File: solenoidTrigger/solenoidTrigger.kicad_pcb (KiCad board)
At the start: 2 copper layers, 88.9 x 88.9 mm, 45 parts, among them J8 CONN_02X03, P1 OSTTC03, P2 OSTTC02, P3 OSTTC08, P4 OSTTC03, P5 OSTTC03, Q1 NMOS_CDS16, Q2 NMOS_CDS16, Q3 NMOS_CDS16, Q4 NMOS_CDS16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

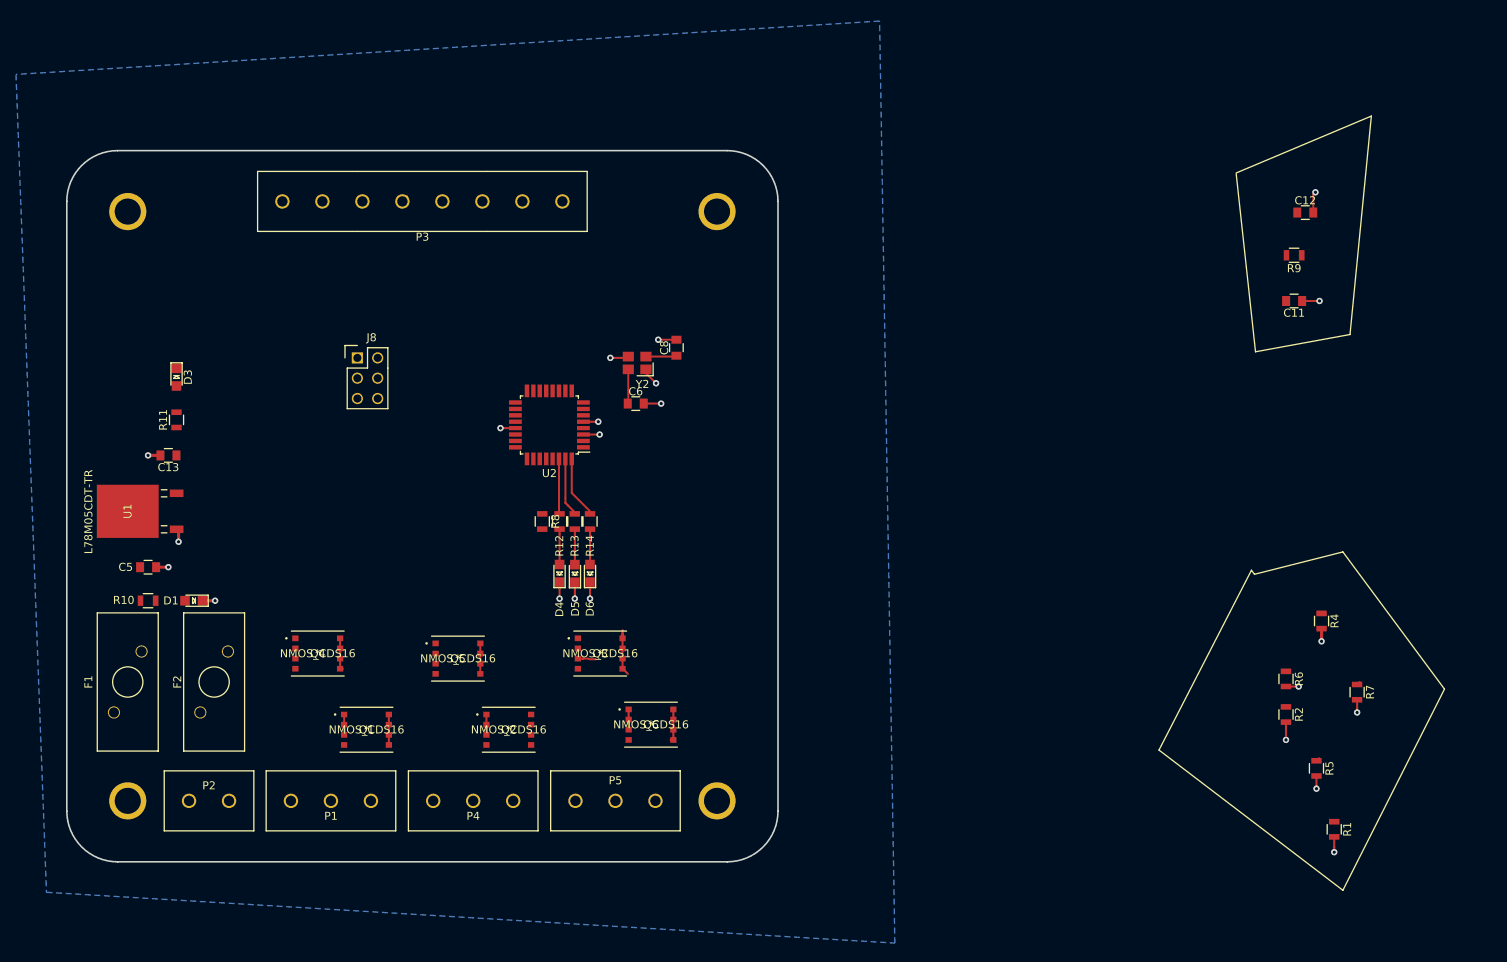
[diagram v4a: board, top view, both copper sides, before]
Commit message: continued moving around components
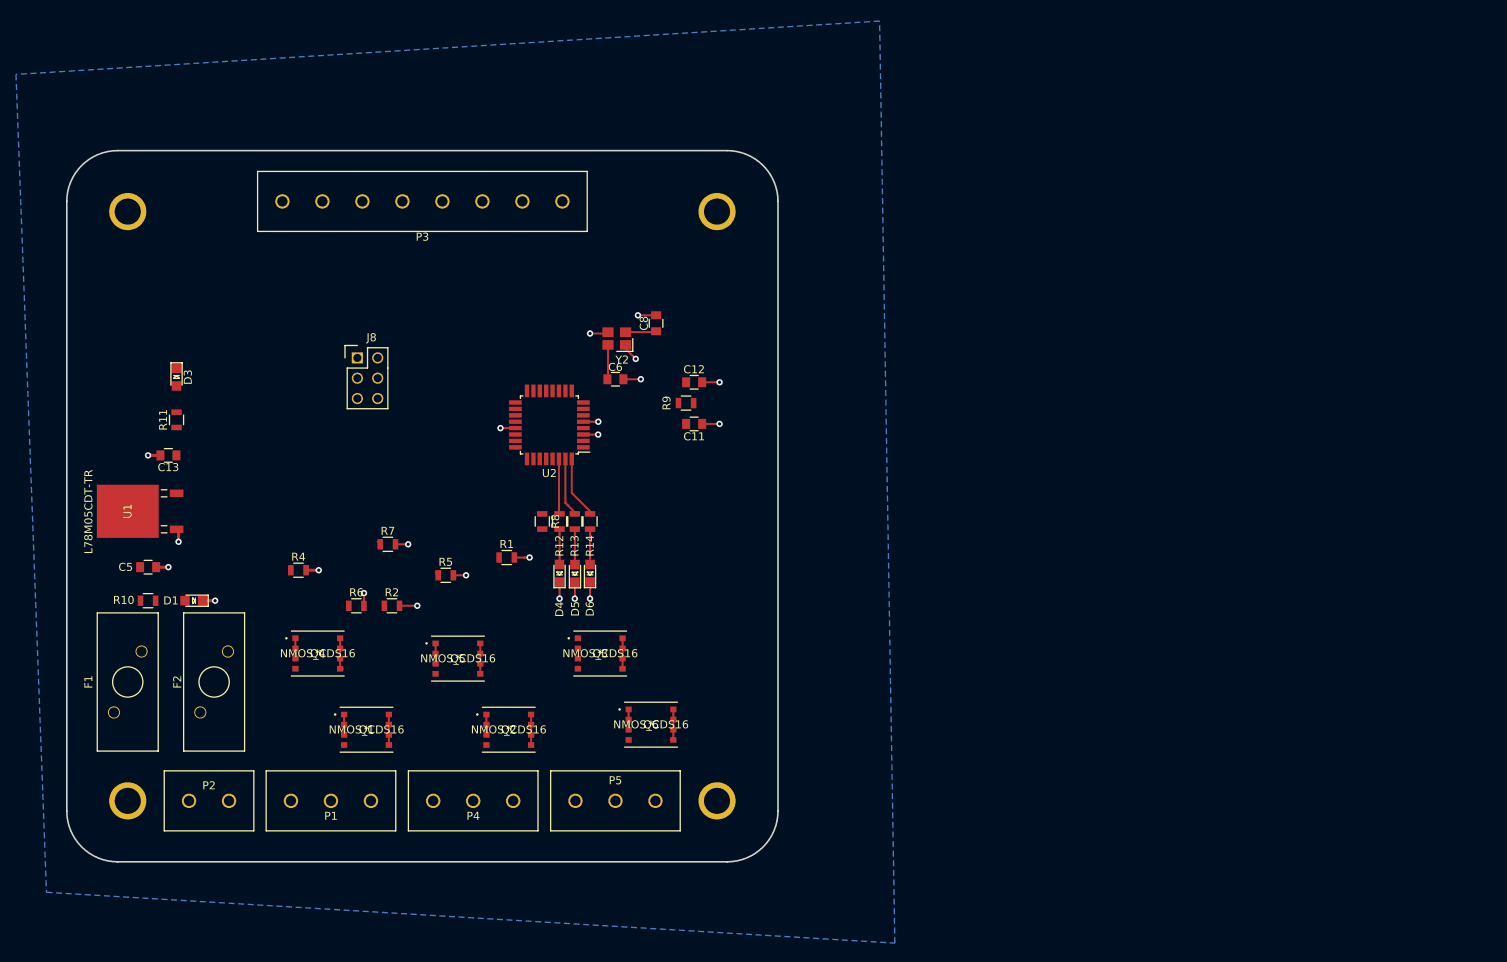
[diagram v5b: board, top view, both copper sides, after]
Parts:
- moved R4 128.0 mm to (131.8, 102.0), turned to 0 degrees
- moved R7 122.6 mm to (143.0, 98.7), turned to 0 degrees
- moved R6 116.6 mm to (139.1, 106.4), turned to 0 degrees
- moved R2 112.6 mm to (143.5, 106.4), turned to 0 degrees
- moved R5 111.5 mm to (150.2, 102.6), turned to 0 degrees
- moved R1 108.9 mm to (157.9, 100.4), turned to 0 degrees
- moved C12 79.3 mm to (181.3, 78.5)
- moved R9 78.2 mm to (180.3, 81.1)
- moved C11 76.6 mm to (181.3, 83.7)
- moved C6 3.97 mm to (171.4, 78.1)
- moved C8 3.97 mm to (176.5, 71.1)
- moved Y2 3.97 mm to (171.6, 73.0)
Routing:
- net /12V_Solenoid2: track 2.54 -> 5.08 mm
- net /12V_Solenoid1: track 2.54 -> 5.08 mm
- net /12V_Solenoid3: track 4.64 -> 2.54 mm
- net /12V_Switch: track 22.4 -> 23.7 mm
- net GND: track 42.8 -> 42.2 mm

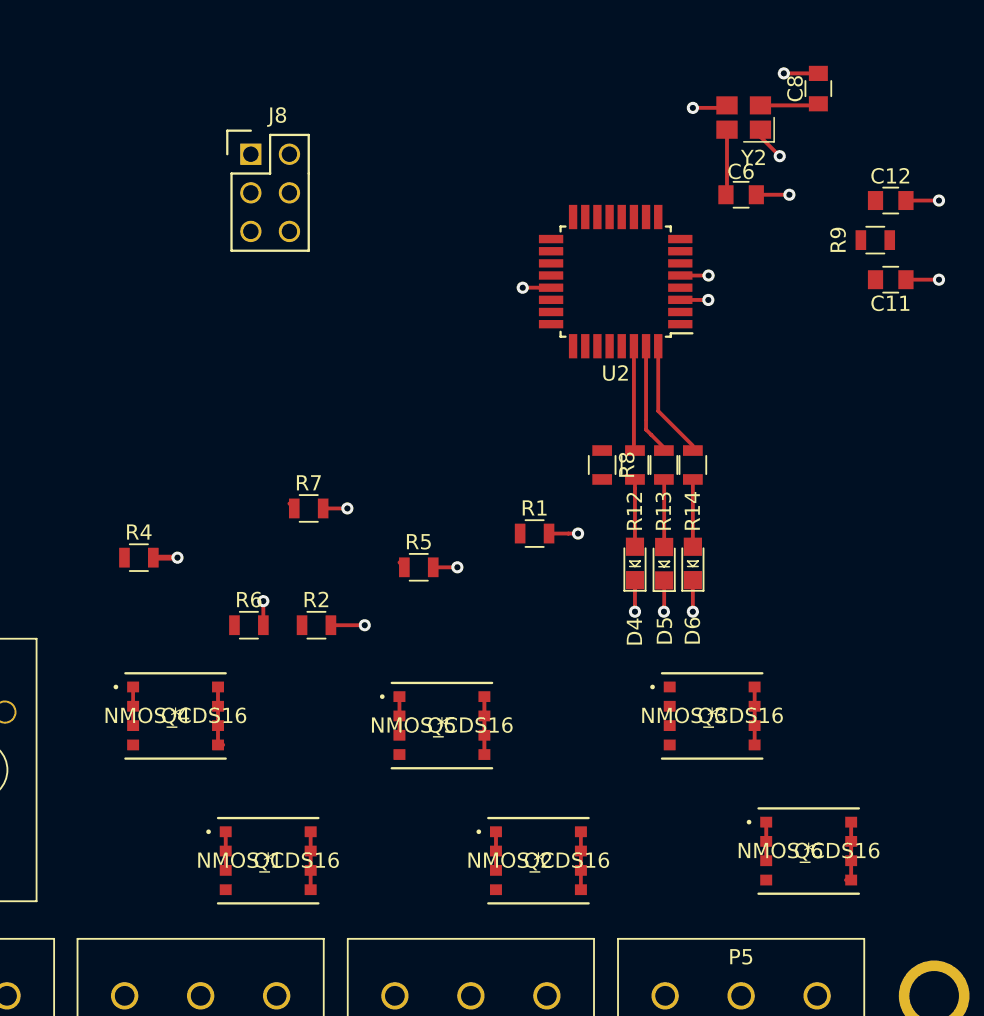
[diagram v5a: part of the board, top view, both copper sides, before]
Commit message: moved all components into what seems to be resonable positions, waiting for confirmation from Will before adding traces/vias
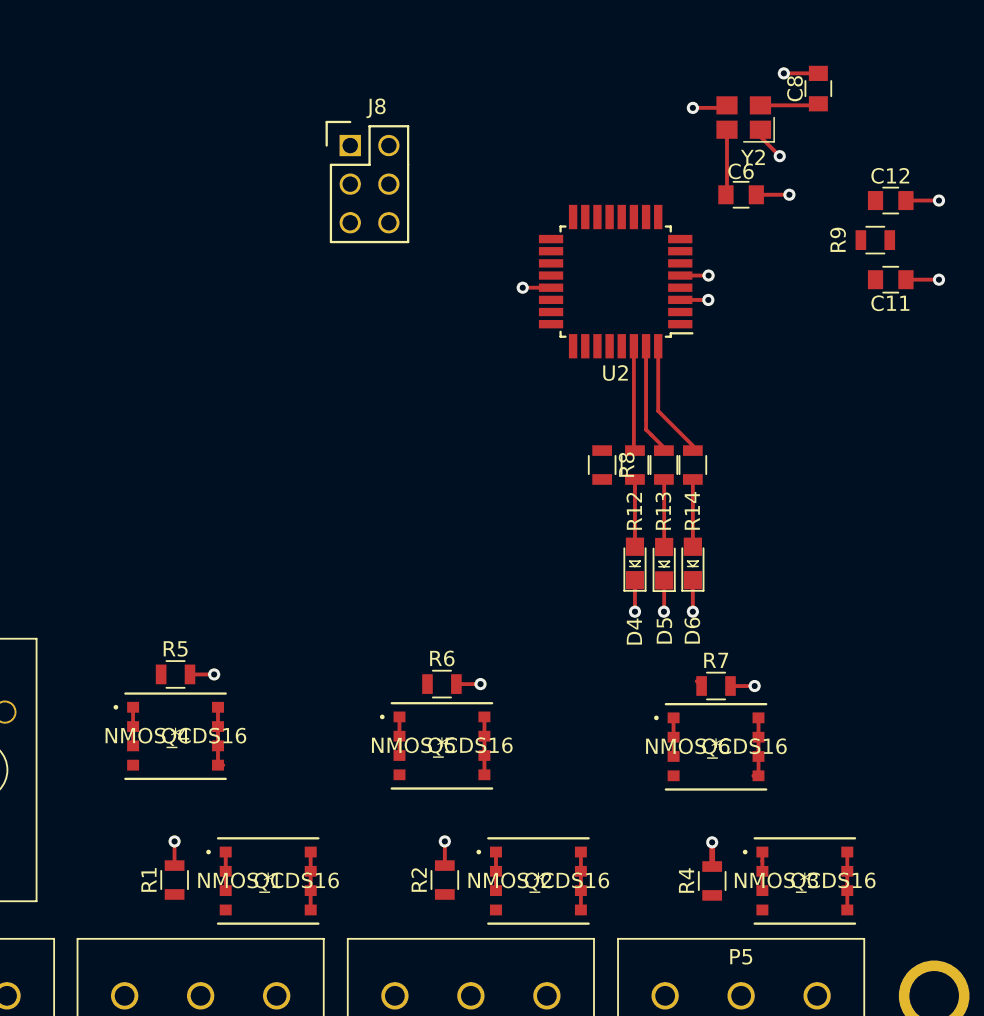
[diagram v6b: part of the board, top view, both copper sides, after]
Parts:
- moved R4 43.3 mm to (169.5, 123.3), turned to 90 degrees
- moved R1 32.9 mm to (134.2, 123.2), turned to 90 degrees
- moved R7 29.2 mm to (169.8, 110.4)
- moved R2 18.8 mm to (152.0, 123.2), turned to 90 degrees
- moved R5 17.5 mm to (134.2, 109.7)
- moved R6 13.3 mm to (151.8, 110.3)
- moved Q3 12.5 mm to (175.6, 123.3)
- moved Q6 9.18 mm to (169.8, 114.4)
- moved J8 6.57 mm to (145.7, 74.9)
- moved Q1 1.33 mm to (140.3, 123.3)
- moved Q2 1.33 mm to (158.1, 123.3)
- moved Q4 1.33 mm to (134.2, 113.7)
- moved Q5 1.33 mm to (151.8, 114.4)
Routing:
- net /12V_Solenoid3: track 2.54 -> 5.08 mm
- net GND: track 42.2 -> 41.2 mm

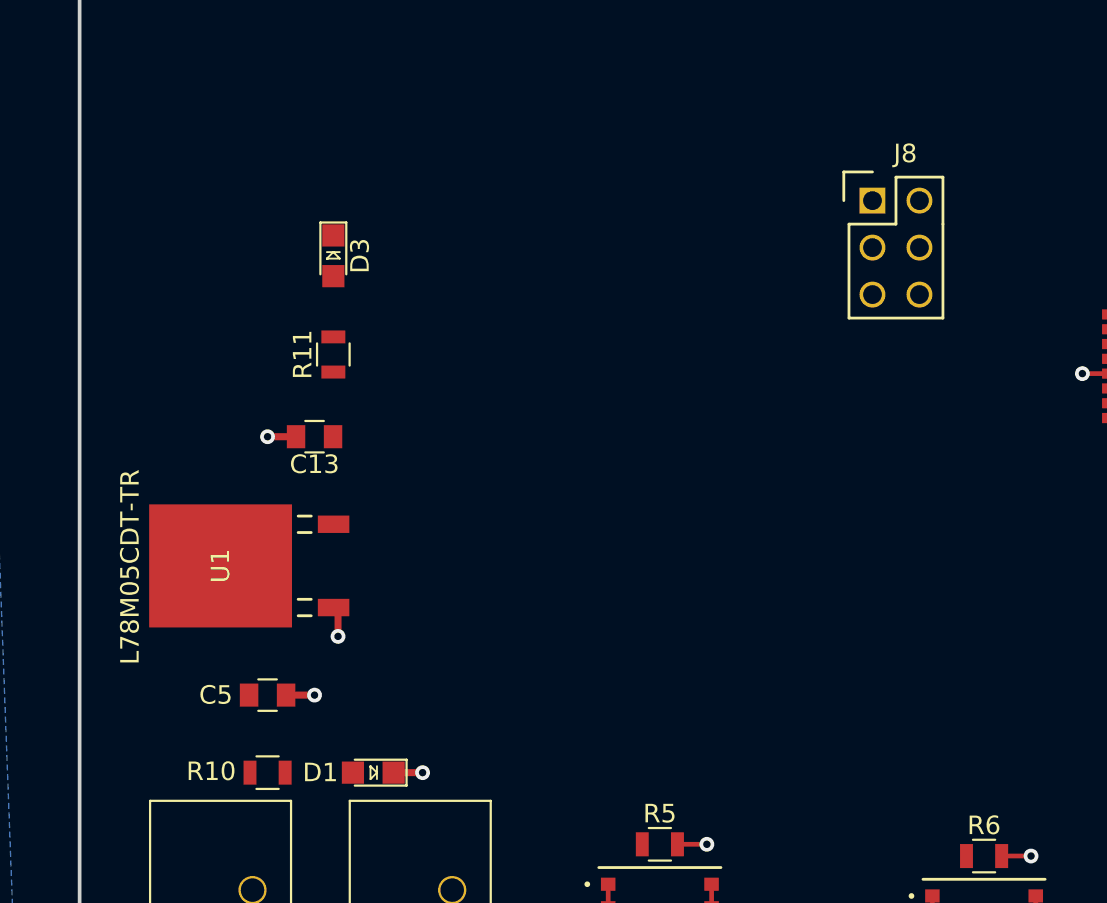
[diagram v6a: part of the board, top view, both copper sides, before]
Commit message: moved linear regulator closer to atmega
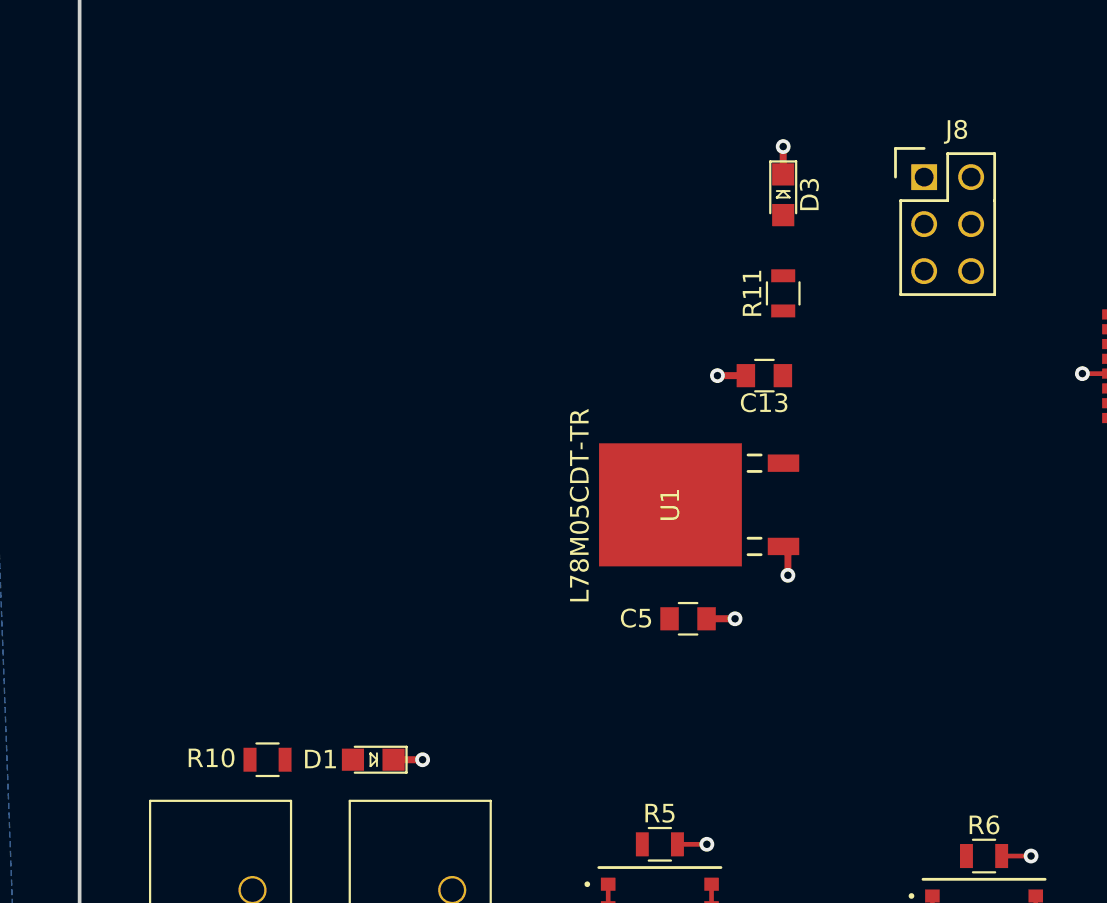
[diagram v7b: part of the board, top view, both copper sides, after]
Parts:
- moved C13 24.5 mm to (139.9, 84.3)
- moved R11 24.5 mm to (140.9, 79.9)
- moved D3 24.5 mm to (140.9, 74.5)
- moved U1 24.5 mm to (134.8, 91.3)
- moved C5 23.1 mm to (135.8, 97.5)
- moved J8 3.07 mm to (148.5, 73.6)
- moved D1 0.70 mm to (118.7, 105.1)
- moved R10 0.70 mm to (113.0, 105.1)
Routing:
- net GND: track 41.2 -> 42.8 mm, vias 22 -> 23
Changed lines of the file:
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@@
     (thickness 1.6)
     (drawings 8)
-    (tracks 111)
+    (tracks 114)
     (zones 0)
     (modules 45)
@@
   )
   (setup
-    (last_trace_width 0.25)
+    (last_trace_width 0.254)
     (user_trace_width 0.254)
     (user_trace_width 0.381)
@@
   )
   (module footprints:Pin_Header_Straight_2x03 (layer F.Cu)
-    (at 145.7325 74.8665)
+    (at 148.5265 73.5965)
     (descr "Through hole pin header")
     (tags "pin header")
@@
   )
   (module footprints:C_0805_OEM (layer F.Cu)
-    (at 115.57 87.63 180)
+    (at 139.8905 84.328 180)
     (descr "Capacitor SMD 0805, reflow soldering, AVX (see smccp.pdf)")
     (tags "capacitor 0805")
@@
   )
   (module footprints:C_0805_OEM (layer F.Cu)
-    (at 113.03 101.6 180)
+    (at 135.763 97.4725 180)
     (descr "Capacitor SMD 0805, reflow soldering, AVX (see smccp.pdf)")
     (tags "capacitor 0805")
@@
   )
   (module footprints:LED_0805_OEM (layer F.Cu)
-    (at 118.745 105.791 180)
+    (at 118.745 105.0925 180)
     (descr "LED 0805 smd package")
     (tags "LED led 0805 SMD smd SMT smt smdled SMDLED smtled SMTLED")
@@
   )
   (module footprints:LED_0805_OEM (layer F.Cu)
-    (at 116.586 77.851 270)
+    (at 140.9065 74.549 270)
     (descr "LED 0805 smd package")
     (tags "LED led 0805 SMD smd SMT smt smdled SMDLED smtled SMTLED")
@@
   )
   (module footprints:R_0805_OEM (layer F.Cu)
-    (at 113.03 105.791)
+    (at 113.03 105.0925)
     (descr "Resistor SMD 0805, reflow soldering, Vishay (see dcrcw.pdf)")
     (tags "resistor 0805")
@@
   )
   (module footprints:R_0805_OEM (layer F.Cu)
-    (at 116.586 83.185 90)
+    (at 140.9065 79.883 90)
     (descr "Resistor SMD 0805, reflow soldering, Vishay (see dcrcw.pdf)")
     (tags "resistor 0805")
@@
   )
   (module footprints:L78M05CDT-TR (layer F.Cu)
-    (at 110.49 94.615 90)
+    (at 134.8105 91.313 90)
     (fp_text reference U1 (at 0 0 90) (layer F.SilkS)
       (effects (font (size 1 1) (thickness 0.15)))
@@
   (gr_line (start 191.77 132.08) (end 191.77 55.88) (layer Edge.Cuts) (width 0.2))
   (segment (start 110.779999 57.3913) (end 110.060099 57.3913) (width 0.254) (layer F.Cu) (net 0))
+  (segment (start 140.9065 73.4855) (end 140.9065 71.9455) (width 0.381) (layer F.Cu) (net 1))
+  (segment (start 140.9065 71.9455) (end 140.9065 71.9455) (width 0.381) (layer F.Cu) (net 1))
+  (via (at 140.9065 71.9455) (size 0.8) (drill 0.4) (layers F.Cu B.Cu) (net 1))
   (segment (start 134.1755 122.24) (end 134.1755 120.65) (width 0.254) (layer F.Cu) (net 1))
   (via (at 134.1755 120.65) (size 0.8) (drill 0.4) (layers F.Cu B.Cu) (net 1))
@@
   (via (at 169.291 85.0265) (size 0.8) (drill 0.4) (layers F.Cu B.Cu) (net 1))
   (segment (start 167.4495 85.0265) (end 169.3145 85.0265) (width 0.254) (layer F.Cu) (net 1))
-  (via (at 121.412 105.791) (size 0.8) (drill 0.4) (layers F.Cu B.Cu) (net 1))
-  (segment (start 119.872 105.791) (end 121.412 105.791) (width 0.381) (layer F.Cu) (net 1))
+  (via (at 121.412 105.0925) (size 0.8) (drill 0.4) (layers F.Cu B.Cu) (net 1))
+  (segment (start 119.872 105.0925) (end 121.412 105.0925) (width 0.381) (layer F.Cu) (net 1))
   (segment (start 172.62 73.825) (end 172.45 73.995) (width 0.254) (layer F.Cu) (net 1))
   (segment (start 172.72 73.825) (end 172.62 73.825) (width 0.254) (layer F.Cu) (net 1))
@@
   (segment (start 135.189 109.6645) (end 136.779 109.6645) (width 0.254) (layer F.Cu) (net 1))
   (segment (start 169.545 122.3035) (end 169.545 120.7135) (width 0.381) (layer F.Cu) (net 1))
-  (via (at 116.84 98.425) (size 0.8) (drill 0.4) (layers F.Cu B.Cu) (net 1))
-  (segment (start 116.84 96.885) (end 116.84 98.425) (width 0.381) (layer F.Cu) (net 1))
-  (segment (start 114.3 101.6) (end 114.3 101.6) (width 0.381) (layer F.Cu) (net 1))
-  (segment (start 114.03 101.6) (end 115.57 101.6) (width 0.381) (layer F.Cu) (net 1))
-  (via (at 115.57 101.6) (size 0.8) (drill 0.4) (layers F.Cu B.Cu) (net 1))
-  (segment (start 114.57 87.63) (end 113.03 87.63) (width 0.381) (layer F.Cu) (net 1))
-  (segment (start 113.03 87.63) (end 113.03 87.63) (width 0.381) (layer F.Cu) (net 1))
-  (via (at 113.03 87.63) (size 0.8) (drill 0.4) (layers F.Cu B.Cu) (net 1))
+  (via (at 141.1605 95.123) (size 0.8) (drill 0.4) (layers F.Cu B.Cu) (net 1))
+  (segment (start 141.1605 93.583) (end 141.1605 95.123) (width 0.381) (layer F.Cu) (net 1))
+  (segment (start 137.033 97.4725) (end 137.033 97.4725) (width 0.381) (layer F.Cu) (net 1))
+  (segment (start 136.763 97.4725) (end 138.303 97.4725) (width 0.381) (layer F.Cu) (net 1))
+  (via (at 138.303 97.4725) (size 0.8) (drill 0.4) (layers F.Cu B.Cu) (net 1))
+  (segment (start 138.8905 84.328) (end 137.3505 84.328) (width 0.381) (layer F.Cu) (net 1))
+  (segment (start 137.3505 84.328) (end 137.3505 84.328) (width 0.381) (layer F.Cu) (net 1))
+  (via (at 137.3505 84.328) (size 0.8) (drill 0.4) (layers F.Cu B.Cu) (net 1))
   (via (at 166.37 105.537) (size 0.8) (drill 0.4) (layers F.Cu B.Cu) (net 1))
   (segment (start 166.259501 105.520499) (end 166.243 105.537) (width 0.25) (layer F.Cu) (net 1))
   (segment (start 166.386501 103.479499) (end 166.386501 105.520499) (width 0.25) (layer F.Cu) (net 1))
   (segment (start 179.9725 78.806) (end 180.2925 78.486) (width 0.254) (layer F.Cu) (net 2))
-  (segment (start 116.57 87.63) (end 116.57 87.755) (width 0.254) (layer F.Cu) (net 2))
+  (segment (start 140.8905 84.328) (end 140.8905 84.453) (width 0.254) (layer F.Cu) (net 2))
   (segment (start 170.52 78.035) (end 170.45 78.105) (width 0.254) (layer F.Cu) (net 4))
   (segment (start 170.45 78.23) (end 170.45 78.105) (width 0.254) (layer F.Cu) (net 4))
